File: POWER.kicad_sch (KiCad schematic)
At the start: 35 parts, among them J4 Conn_01x02_Pin, U1 LM3670MF, U4 BQ24230RGT, U5 LM3670MF, U6 LM3670MF

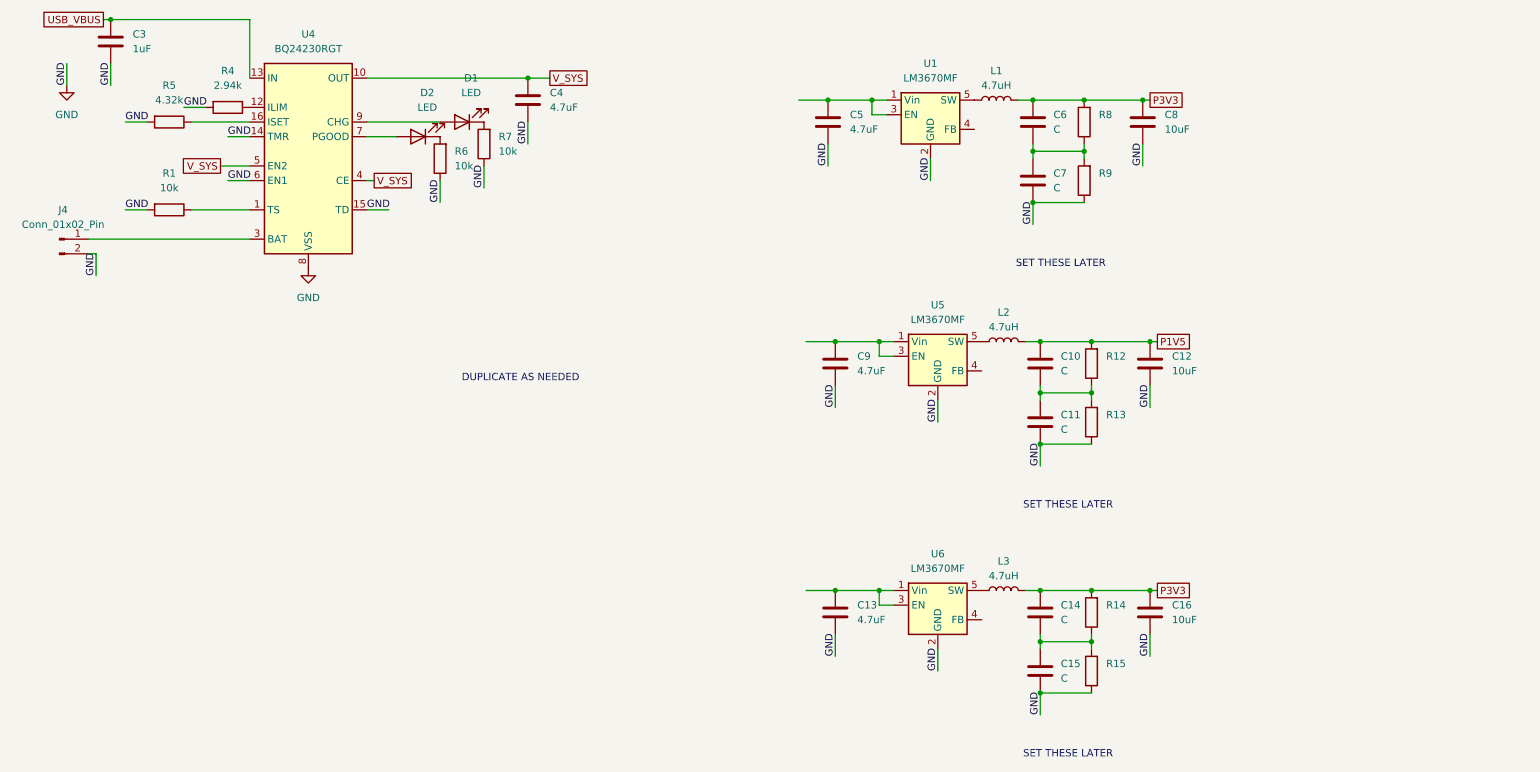
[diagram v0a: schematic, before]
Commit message: Changed power regulators, filled out DRAM, begin changing FPGA from ECP5 to ICE40
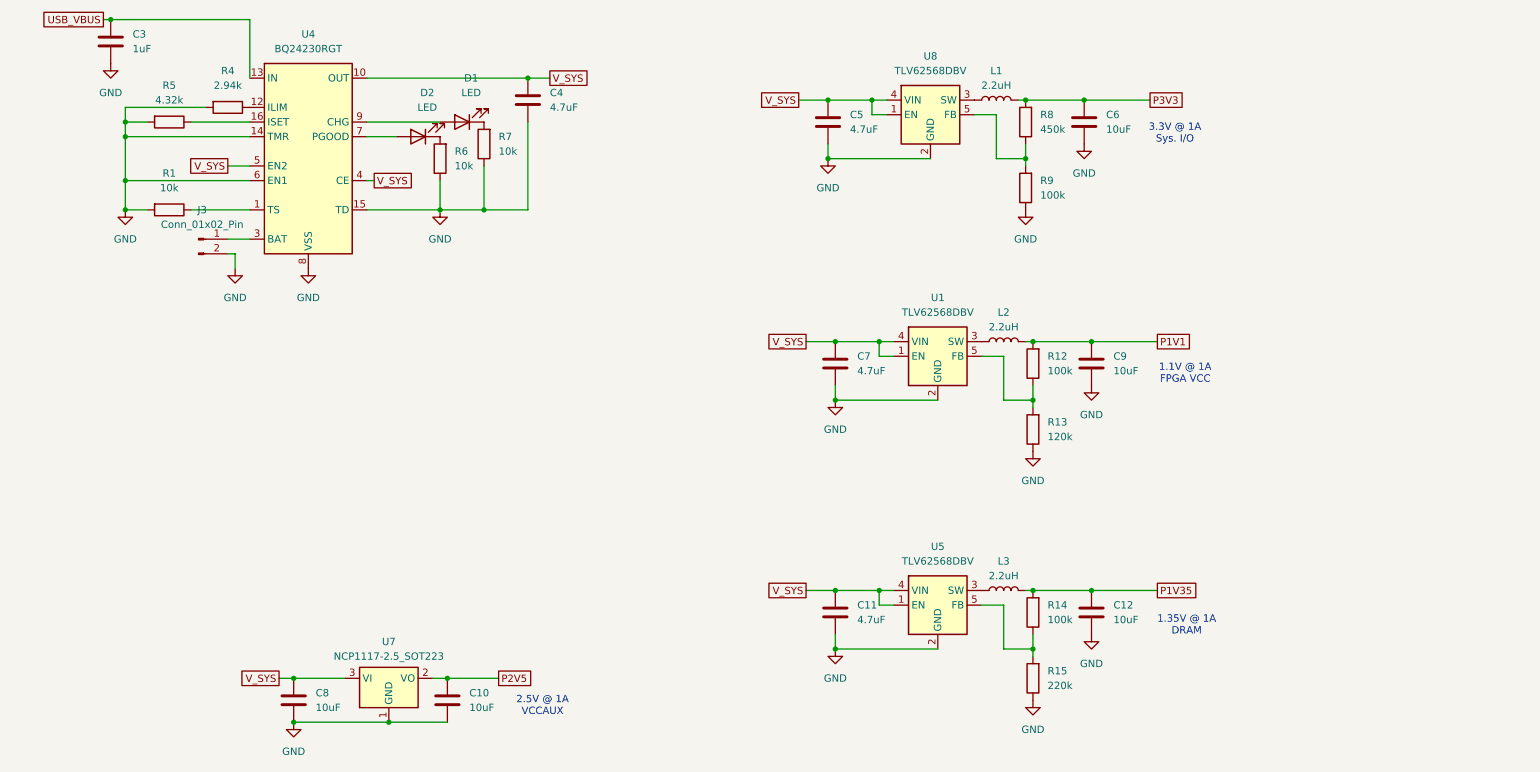
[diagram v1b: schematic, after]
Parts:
- removed C13: 4.7uF, symbol Device:C
- removed C14, C15: C, symbol Device:C
- removed C16: 10uF, symbol Device:C
- removed J4: Conn_01x02_Pin, Connector_JST:JST_PH_B2B-PH-K_1x02_P2.00mm_Vertical, symbol Connector:Conn_01x02_Pin
- removed U1, U5, U6: LM3670MF, Package_TO_SOT_SMD:TSOT-23-5, symbol Regulator_Switching:LM3670MF
- added J3: Conn_01x02_Pin, Connector_JST:JST_PH_B2B-PH-K_1x02_P2.00mm_Vertical, symbol Connector:Conn_01x02_Pin
- added U1, U5, U8: TLV62568DBV, Package_TO_SOT_SMD:SOT-23-5, symbol Regulator_Switching:TLV62568DBV
- added U7: NCP1117-2.5_SOT223, Package_TO_SOT_SMD:SOT-223-3_TabPin2, symbol Regulator_Linear:NCP1117-2.5_SOT223
- C10, C6: value C -> 10uF
- C11, C7: value C -> 4.7uF
- C9: value 4.7uF -> 10uF
- L1, L2, L3: value 4.7uH -> 2.2uH
- R12, R14, R9: value ~ -> 100k
- R13: value ~ -> 120k
- R15: value ~ -> 220k
- R8: value ~ -> 450k
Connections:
- net GND: now also C10.2, C6.2, J3.2 (Pin_2), U1.2 (GND), U5.2 (GND), U7.1 (GND), U8.2 (GND)
- net P3V3: no longer C8.1, L3.2, R14.2
- net V_SYS: now also C11.1, C5.1, C7.1, C8.1, U1.1 (EN), U1.4 (VIN), U5.1 (EN), U5.4 (VIN), U7.3 (VI), U8.1 (EN), U8.4 (VIN)
- net at R12.1, R13.2: now also U1.5 (FB); no longer C10.2, C11.1
- net at L1.1: now also U8.3 (SW)
- net at L3.1: now also U5.3 (SW)
- net at R8.1, R9.2: now also U8.5 (FB); no longer C6.2, C7.1
- net at L2.1: now also U1.3 (SW)
- net P1V1: now reaches C9.1
- net P1V1: now also L2.2, R12.2
- net at U4.2 (BAT), U4.3 (BAT): now also J3.1 (Pin_1)
- net at R14.1, R15.2: now also U5.5 (FB)
- removed net P1V5: C10.1, C12.1, L2.2, R12.2
- new net P1V35: C12.1, L3.2, R14.2
- new net P2V5: C10.1, U7.2 (VO)
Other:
- note added: "1.1V @ 1A FPGA VCC"
- note added: "1.35V @ 1A DRAM"
- note added: "2.5V @ 1A VCCAUX"
- note added: "3.3V @ 1A Sys. I/O"
- note removed: "DUPLICATE AS NEEDED"
- note removed: "SET THESE LATER"
- moved on the sheet: R8, R9

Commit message: Saving before changing RAM from DDR3 to Parallel SDR SRAM
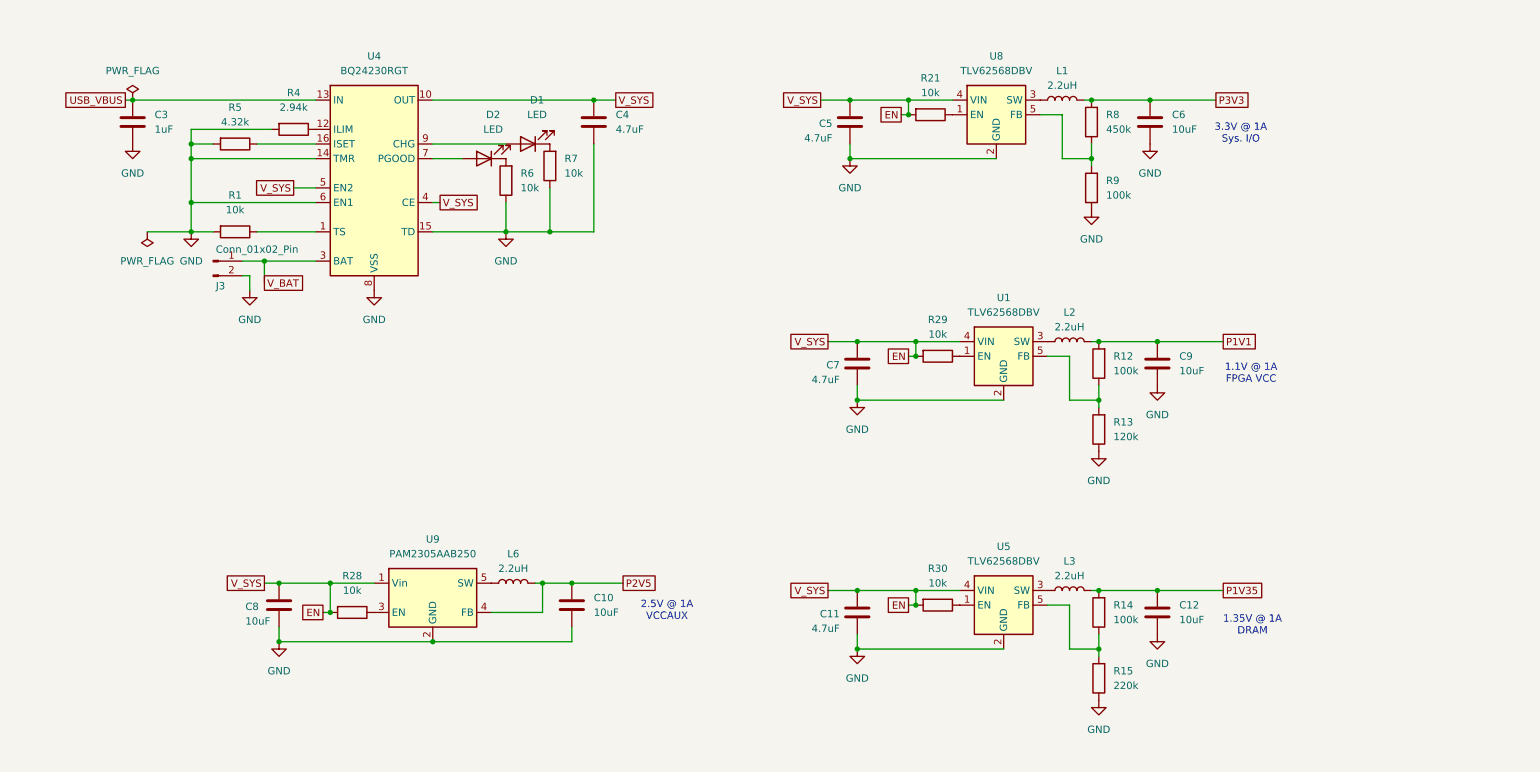
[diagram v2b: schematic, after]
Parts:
- removed U7: NCP1117-2.5_SOT223, Package_TO_SOT_SMD:SOT-223-3_TabPin2, symbol Regulator_Linear:NCP1117-2.5_SOT223
- added L6: 2.2uH, symbol Device:L
- added R21, R28, R29, R30: 10k, symbol Device:R
- added U9: PAM2305AAB250, Package_TO_SOT_SMD:TSOT-23-5, symbol Regulator_Switching:PAM2305AAB250
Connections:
- net GND: now also U9.2 (GND)
- net P2V5: now also L6.2, U9.4 (FB)
- net V_BAT: now reaches J3.1 (Pin_1), U4.2 (BAT), U4.3 (BAT)
- net V_SYS renamed EN
- net EN: now also R21.2, R28.2, R29.2, R30.2, U9.1 (Vin); no longer U1.1 (EN), U5.1 (EN), U8.1 (EN)
- new net: R30.1, U5.1 (EN)
- new net: R29.1, U1.1 (EN)
- new net: R21.1, U8.1 (EN)
- new net: R28.1, U9.3 (EN)
- new net: L6.1, U9.5 (SW)
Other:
- moved on the sheet: C10, C11, C12, C3, C4, C5, C6, C7, C8, C9, D1, D2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

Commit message: Added more I/O. Changed power regulators
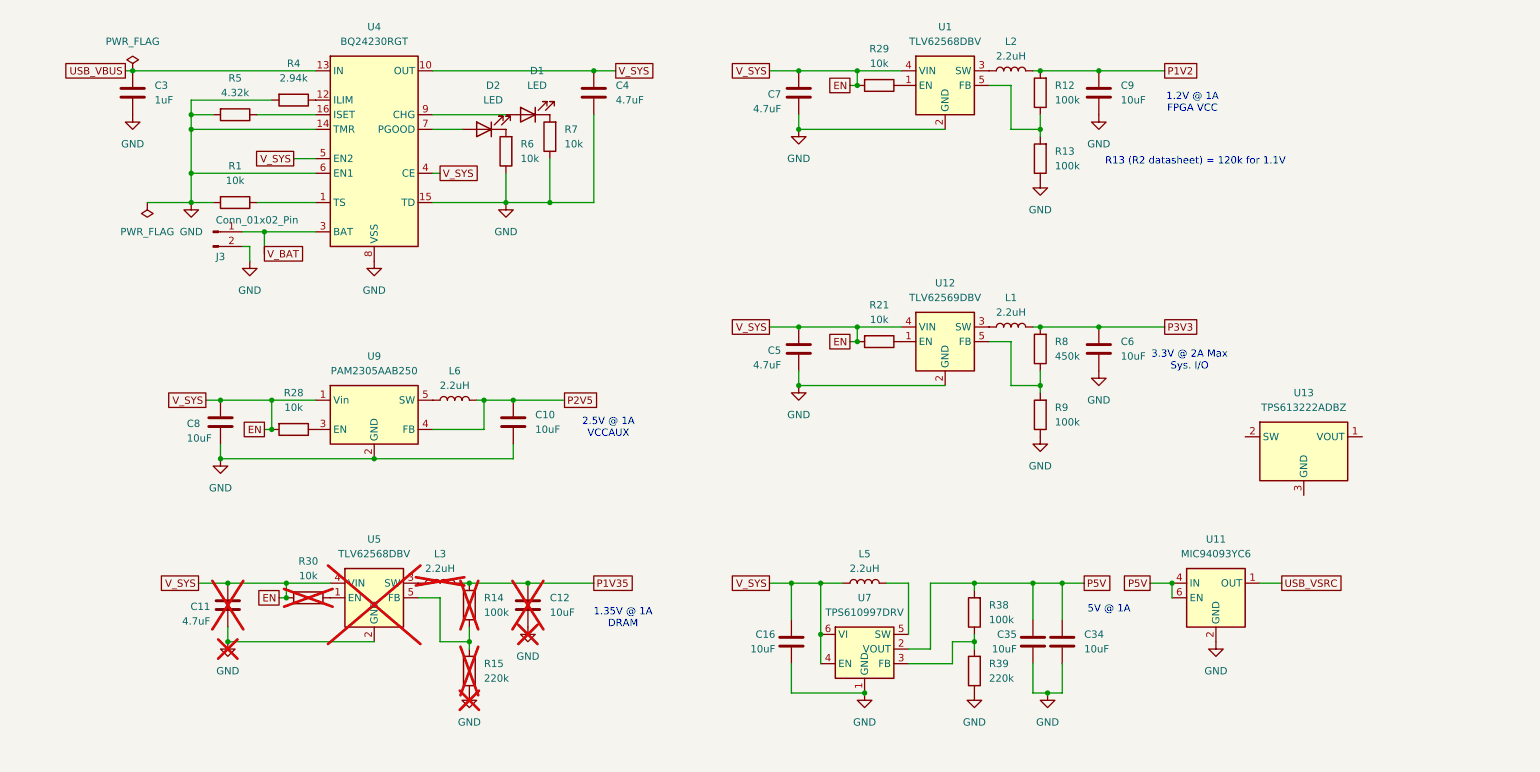
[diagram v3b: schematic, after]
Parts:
- removed U8: TLV62568DBV, Package_TO_SOT_SMD:SOT-23-5, symbol Regulator_Switching:TLV62568DBV
- added C16, C34, C35: 10uF, symbol Device:C
- added L5: 2.2uH, symbol Device:L
- added R38: 100k, symbol Device:R
- added R39: 220k, symbol Device:R
- added U11: MIC94093YC6, Package_TO_SOT_SMD:SOT-363_SC-70-6, symbol Power_Management:MIC94093YC6
- added U12: TLV62569DBV, Package_TO_SOT_SMD:SOT-23-5, symbol Regulator_Switching:TLV62569DBV
- added U13: TPS613222ADBZ, Package_TO_SOT_SMD:SOT-23, symbol Regulator_Switching:TPS613222ADBZ
- added U7: TPS610997DRV, Package_SON:WSON-6-1EP_2x2mm_P0.65mm_EP1x1.6mm, symbol Regulator_Switching:TPS610997DRV
- C11, C12, L3, R14, R15, R30, U5: now not fitted
- R13: value 120k -> 100k
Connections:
- net EN: now also C16.1, L5.1, U12.4 (VIN), U7.4 (EN), U7.6 (VI)
- net GND: now also C16.2, C34.2, C35.2, R39.1, U11.2 (GND), U11.5 (GND), U12.2 (GND), U7.1 (GND), U7.7 (GND)
- net at R21.1: now also U12.1 (EN)
- net at L1.1: now also U12.3 (SW)
- net at R8.1, R9.2: now also U12.5 (FB)
- net P1V1 renamed P1V2
- new net: R38.1, R39.2, U7.3 (FB)
- new net: L5.2, U7.5 (SW)
- new net P5V: C34.1, C35.1, R38.2, U11.4 (IN), U11.6 (EN), U7.2 (VOUT)
- new net USB_VSRC: U11.1 (OUT)
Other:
- note added: "1.2V @ 1A FPGA VCC"
- note added: "3.3V @ 2A Max Sys. I/O"
- note added: "5V @ 1A"
- note added: "R13 (R2 datasheet) = 120k for 1.1V"
- note removed: "1.1V @ 1A FPGA VCC"
- note removed: "3.3V @ 1A Sys. I/O"
- moved on the sheet: C10, C3, C4, C5, C6, C7, C8, C9, D1, D2, J3, L1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

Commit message: Power routed. Saving before reworking ICE40 pins to optimize layout
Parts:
- removed C11: 4.7uF, symbol Device:C
- removed C12: 10uF, symbol Device:C
- removed C3: 1uF, symbol Device:C
- removed D1: LED, symbol Device:LED
- removed L5: 2.2uH, symbol Device:L
- removed R1, R28, R30: 10k, symbol Device:R
- removed R14: 100k, symbol Device:R
- removed R15: 220k, symbol Device:R
- removed U12: TLV62569DBV, Package_TO_SOT_SMD:SOT-23-5, symbol Regulator_Switching:TLV62569DBV
- removed U13: TPS613222ADBZ, Package_TO_SOT_SMD:SOT-23, symbol Regulator_Switching:TPS613222ADBZ
- removed U4: BQ24230RGT, Package_DFN_QFN:VQFN-16-1EP_3x3mm_P0.5mm_EP1.68x1.68mm_ThermalVias, symbol Power_Management:BQ24230RGT
- removed U5: TLV62568DBV, Package_TO_SOT_SMD:SOT-23-5, symbol Regulator_Switching:TLV62568DBV
- removed U7: TPS610997DRV, Package_SON:WSON-6-1EP_2x2mm_P0.65mm_EP1x1.6mm, symbol Regulator_Switching:TPS610997DRV
- removed U9: PAM2305AAB250, Package_TO_SOT_SMD:TSOT-23-5, symbol Regulator_Switching:PAM2305AAB250
- added C45: 4.7uF, Capacitor_SMD:C_0603_1608Metric, symbol Device:C
- added C64: 1uF, Capacitor_SMD:C_0603_1608Metric, symbol Device:C
- added D6: LED, LED_SMD:LED_0603_1608Metric, symbol Device:LED
- added R53, R54, R55: 10k, Resistor_SMD:R_0603_1608Metric, symbol Device:R
- added U10: PAM2305AAB250, Package_TO_SOT_SMD:TSOT-23-5, symbol Regulator_Switching:PAM2305AAB250
- added U11: TLV62569DBV, Package_TO_SOT_SMD:SOT-23-5, symbol Regulator_Switching:TLV62569DBV
- added U4: TLV61070ADBV, Package_TO_SOT_SMD:SOT-23-6, symbol Regulator_Switching:TLV61070ADBV
- added U9: BQ24230RGT, Package_DFN_QFN:VQFN-16-1EP_3x3mm_P0.5mm_EP1.68x1.68mm_ThermalVias, symbol Power_Management:BQ24230RGT
- C10, C16, C4, C5, C6, C7, C8, C9: footprint (none) -> Capacitor_SMD:C_0603_1608Metric
- C34, C35: value 10uF -> 22uF; footprint (none) -> Capacitor_SMD:C_0603_1608Metric
- D2: footprint (none) -> LED_SMD:LED_0603_1608Metric
- L1, L2: footprint (none) -> Inductor_SMD:L_Neosid_SMS-ME3010
- L3: footprint (none) -> Inductor_SMD:L_Neosid_SMS-ME3010; now fitted
- L6: footprint (none) -> Inductor_SMD:L_0603_1608Metric
- R12, R13, R21, R29, R4, R5, R6, R7, R8, R9: footprint (none) -> Resistor_SMD:R_0603_1608Metric
- R38: value 100k -> 560k; footprint (none) -> Resistor_SMD:R_0603_1608Metric
- R39: value 220k -> 62k; footprint (none) -> Resistor_SMD:R_0603_1608Metric
- renumbered U11 to U12
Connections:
- net EN: now also R21.1, R29.1, U1.1 (EN), R54.2, R55.2, U10.3 (EN), U11.1 (EN), U4.3 (EN); no longer C16.1, C4.1, C5.1, C7.1, C8.1, R21.2, R29.2, U1.4 (VIN)
- net GND: now also C45.2, C64.2, R53.2, U10.2 (GND), U11.2 (GND), U4.2 (GND), U9.14 (TMR), U9.15 (TD), U9.17 (VSS), U9.4 (CE), U9.6 (EN1), U9.8 (VSS); no longer R6.1, R7.1
- net P2V5: now also U10.4 (FB)
- net P5V: now also U4.5 (V_{OUT})
- net USB_VBUS: now also C64.1, U9.13 (IN)
- net V_BAT: now also C45.1, U9.2 (BAT), U9.3 (BAT)
- net V_SYS: now reaches L3.1
- net V_SYS: now also C16.1, C4.1, C5.1, C7.1, C8.1, R21.2, R29.2, R6.2, R7.2, U1.4 (VIN), R54.1, R55.1, U10.1 (Vin), U11.4 (VIN), U4.6 (V_{IN}), U9.10 (OUT), U9.11 (OUT), U9.5 (EN2)
- net at D2.1 (K): now also U9.7 (PGOOD); no longer R6.2
- net at R5.1: now also U9.16 (ISET)
- net at R38.1, R39.2: now also U4.4 (V_{FB})
- net at L6.1: now also U10.5 (SW)
- net at R4.1: now also U9.12 (ILIM)
- net at D2.2 (A): now also R7.1
- net at L1.1: now also U11.3 (SW)
- net at R8.1, R9.2: now also U11.5 (FB)
- net P1V35: no longer names the net of L3.2
- net P1V35: now also U4.1 (SW)
- net USB_VSRC renamed USB_VBUS2
- new net: D6.2 (A), R6.1
- new net: R53.1, U9.1 (TS)
- new net: D6.1 (K), U9.9 (CHG)
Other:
- note removed: "1.35V @ 1A DRAM"
- moved on the sheet: C16, C34, C35, R29, R38, R39, U12
